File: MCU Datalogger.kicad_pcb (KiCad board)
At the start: 2 copper layers, 0 parts

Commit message: Completed placement of footprints
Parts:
- added BT1: Battery, Connector_PinHeader_2.54mm:PinHeader_1x02_P2.54mm_Vertical, F.Cu at (28.6, 60.3)
- added C1: 0.1uF, Capacitor_SMD:C_0805_2012Metric, F.Cu at (46.4, 55.2)
- added C2: 22pF, Capacitor_SMD:C_0805_2012Metric, F.Cu at (61.9, 76.2)
- added C3: 22pF, Capacitor_SMD:C_0805_2012Metric, F.Cu at (51.4, 55.2)
- added C4: 0.1uF, Capacitor_SMD:C_0805_2012Metric, F.Cu at (61.9, 72.4)
- added C5: 100nF, Capacitor_SMD:C_0805_2012Metric, F.Cu at (56.8, 55.2)
- added D1: LED, LED_SMD:LED_0805_2012Metric, F.Cu at (62.2, 55.2)
- added D2: LED, LED_SMD:LED_0805_2012Metric, F.Cu at (67.0, 55.2)
- added H1: MountingHole, MountingHole:MountingHole_2.1mm, F.Cu at (29.2, 54.6)
- added H2: MountingHole, MountingHole:MountingHole_2.1mm, F.Cu at (29.2, 80.0)
- added H3: MountingHole, MountingHole:MountingHole_2.1mm, F.Cu at (74.9, 54.6)
- added H4: MountingHole, MountingHole:MountingHole_2.1mm, F.Cu at (74.9, 80.0)
- added J1: Conn_01x04_Pin, Connector_PinHeader_2.54mm:PinHeader_1x04_P2.54mm_Vertical, F.Cu at (75.6, 67.9)
- added J2: Conn_01x09_Pin, Connector_PinHeader_2.54mm:PinHeader_1x09_P2.54mm_Vertical, F.Cu at (34.9, 80.6)
- added J3: Conn_01x04_Pin, Connector_PinHeader_2.54mm:PinHeader_1x04_P2.54mm_Vertical, F.Cu at (60.3, 80.6)
- added J4: Conn_02x03_Odd_Even, Connector_PinHeader_2.54mm:PinHeader_2x03_P2.54mm_Vertical, F.Cu at (73.0, 59.1)
- added R1: 10K, Resistor_SMD:R_0805_2012Metric, F.Cu at (35.6, 76.8)
- added R2: 10K, Resistor_SMD:R_0805_2012Metric, F.Cu at (41.6, 76.8)
- added R3: 4.7K, Resistor_SMD:R_0805_2012Metric, F.Cu at (62.0, 68.6)
- added R4: 4.7K, Resistor_SMD:R_0805_2012Metric, F.Cu at (62.0, 64.1)
- added R5: 330, Resistor_SMD:R_0805_2012Metric, F.Cu at (67.0, 60.3)
- added R6: 10K, Resistor_SMD:R_0805_2012Metric, F.Cu at (67.0, 64.1)
- added R7: 330, Resistor_SMD:R_0805_2012Metric, F.Cu at (62.0, 60.3)
- added U1: DS1337S_, DS1337S_:SOIC127P600X175-8N, F.Cu at (38.7, 71.8)
- added U2: 24LC1025, Package_SO:SOIC-8_5.3x5.3mm_P1.27mm, F.Cu at (38.5, 56.5)
- added U3: 24LC1025, Package_SO:SOIC-8_5.3x5.3mm_P1.27mm, F.Cu at (38.7, 64.8)
- added U4: ATMEGA328P-AU, ATMEGA328P-AU:QFP80P900X900X120-32N, F.Cu at (51.2, 65.7)
- added Y1: 32.768 KHz, Crystal:Crystal_SMD_5032-2Pin_5.0x3.2mm_HandSoldering, F.Cu at (29.8, 71.1)
- added Y2: 16 MHz, Crystal:Crystal_SMD_5032-2Pin_5.0x3.2mm_HandSoldering, F.Cu at (51.4, 74.9)
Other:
- board outline added: 50.8 x 30.5 mm

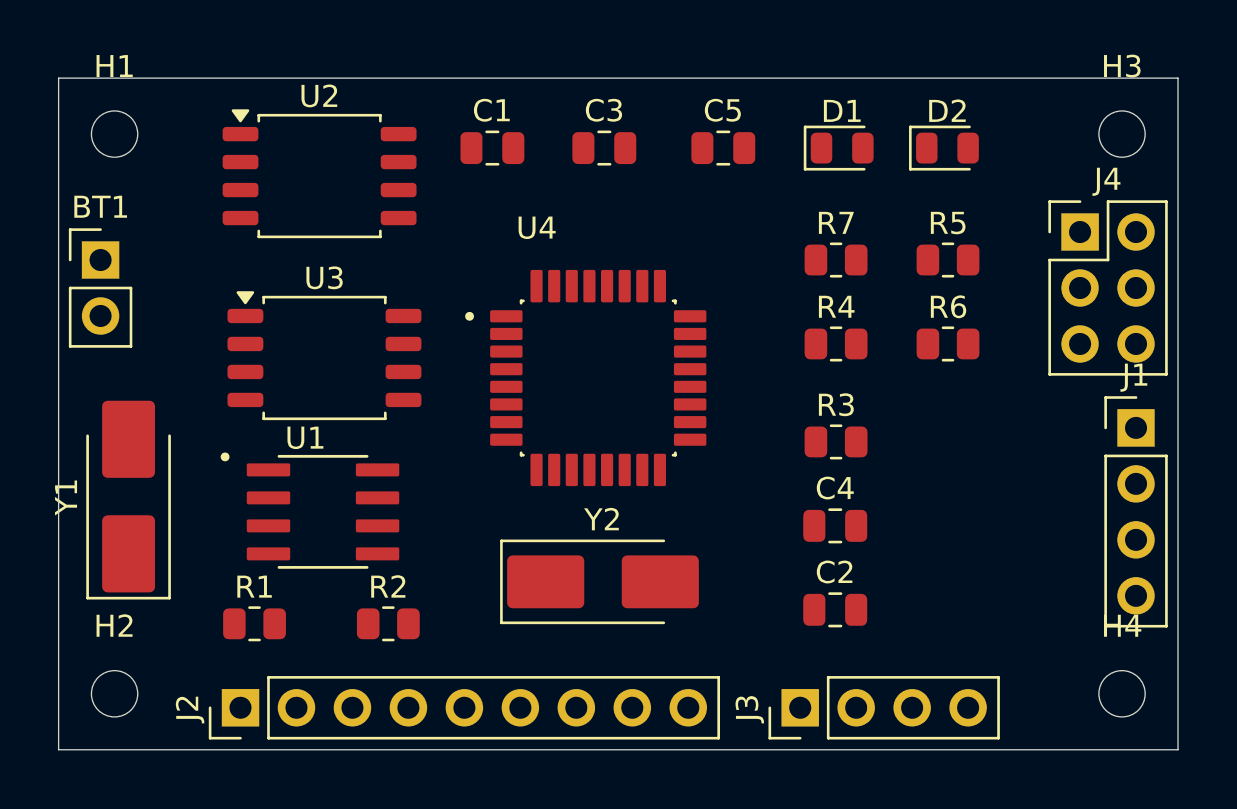
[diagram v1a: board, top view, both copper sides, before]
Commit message: Refined and completed outline
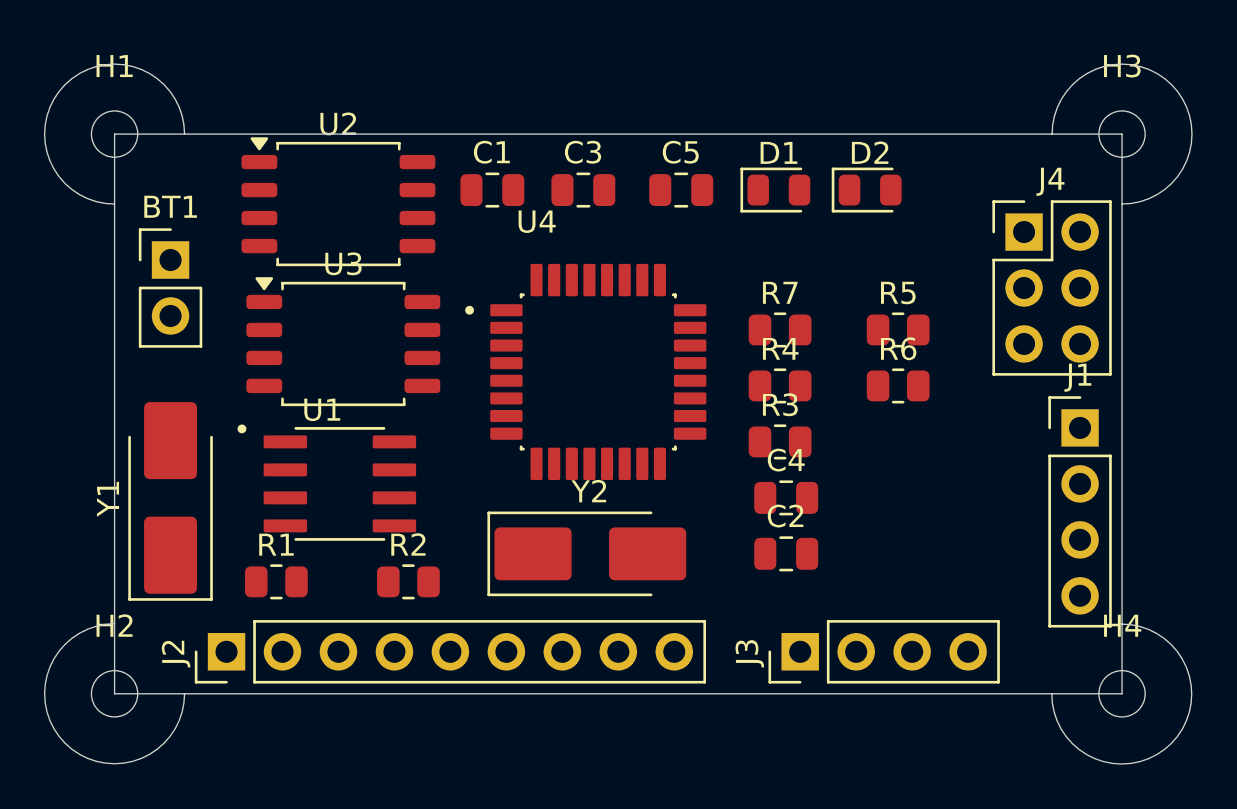
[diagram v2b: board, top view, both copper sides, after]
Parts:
- moved R7 4.07 mm to (59.4, 63.5)
- moved D2 3.99 mm to (63.5, 57.1)
- moved R5 3.90 mm to (64.8, 63.5)
- moved D1 3.45 mm to (59.4, 57.1)
- moved C2 3.38 mm to (59.7, 73.7)
- moved BT1 3.18 mm to (31.8, 60.3)
- moved R4 3.18 mm to (59.4, 66.0)
- moved R6 2.96 mm to (64.8, 66.0)
- moved C5 2.70 mm to (54.9, 57.1)
- moved J2 2.62 mm to (34.3, 78.1)
- moved C4 2.56 mm to (59.7, 71.1)
- moved J4 2.54 mm to (70.5, 59.1)
- moved R3 2.54 mm to (59.4, 68.6)
- moved J1 2.54 mm to (73.0, 67.9)
- moved J3 2.54 mm to (60.3, 78.1)
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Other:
- board size 50.8 x 30.5 mm -> 52.1 x 31.8 mm

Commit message: Ready to manufacture version 1
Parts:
- added REF**: KiCad-Logo2_5mm_SilkScreen, Symbol:KiCad-Logo2_5mm_SilkScreen, B.Cu at (58.1, 63.0)
- moved D1 4.78 mm to (64.1, 57.1)
- moved D2 4.14 mm to (59.4, 57.1)
- moved R3 2.82 mm to (62.2, 68.6), turned to 180 degrees
- moved R4 2.82 mm to (62.2, 66.0), turned to 180 degrees
- moved R7 2.82 mm to (62.2, 63.5), turned to 180 degrees
- moved C2 2.54 mm to (62.2, 73.7)
- moved C4 2.54 mm to (62.2, 71.1)
- moved Y2 1.91 mm to (52.7, 73.7), turned to 180 degrees
- moved R6 1.63 mm to (66.4, 66.0), turned to 180 degrees
- moved R5 1.55 mm to (66.3, 63.5)
- moved U4 1.48 mm to (52.6, 65.7)
- moved R2 0.64 mm to (41.9, 74.9)
- moved R1 0.28 mm to (36.8, 74.9), turned to 180 degrees
- turned C1 to 180 degrees
- turned C3 to 180 degrees
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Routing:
- net /Vcc: track 0.00 -> 88.7 mm, vias 0 -> 8
- net /SCK: track 0.00 -> 82.0 mm, vias 0 -> 4
- net /SDA: track 0.00 -> 58.3 mm, vias 0 -> 2
- net GND: track 0.00 -> 36.5 mm, vias 0 -> 10
- net /TX: track 0.00 -> 31.4 mm, vias 0 -> 2
- net /D2: track 0.00 -> 29.8 mm, vias 0 -> 2
- net /RX: track 0.00 -> 28.0 mm, vias 0 -> 2
- net /D3: track 0.00 -> 24.5 mm, vias 0 -> 2
- net /MOSI: track 0.00 -> 24.4 mm, vias 0 -> 1
- net /RESET: track 0.00 -> 23.5 mm
- net Net-(U4-PB7): track 0.00 -> 23.4 mm, vias 0 -> 2
- net /D4: track 0.00 -> 21.2 mm, vias 0 -> 2
- net /MISO: track 0.00 -> 21.1 mm, vias 0 -> 1
- net Net-(U4-PB6): track 0.00 -> 19.4 mm
- net Net-(U4-AREF): track 0.00 -> 13.6 mm
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- added copper zone on F.Cu, net /Vcc
- added copper zone on B.Cu, net GND
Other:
- outline, holes or cut-outs redrawn
- board text added: "2"
- board text added: "3"
- board text added: "4"
- board text added: "5"
- board text added: "6"
- board text added: "7"
- board text added: "8"
- board text added: "Data logger with ATMega328P. - 2Mbit EEPROM - RTC - I2C, SPI, GPIO"
- board text added: "GND"
- board text added: "GPIO"
- board text added: "I2C"
- board text added: "ICSP"
- board text added: "RX"
- board text added: "SCK"
- board text added: "SDA"
- board text added: "SERIAL"
- board text added: "TX"
- board text added: "Vcc"
